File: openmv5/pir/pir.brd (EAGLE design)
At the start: 35.6 x 26.7 mm, 57 parts, among them IC1 AP3032KTR-G1, IC2 AP3032KTR-G1, J1 OPENMV5-TOP, Q1 2N7002KW_R1_00001, U1 EKMB1307113K, U2 MIC5365-3.3YMT-TZ

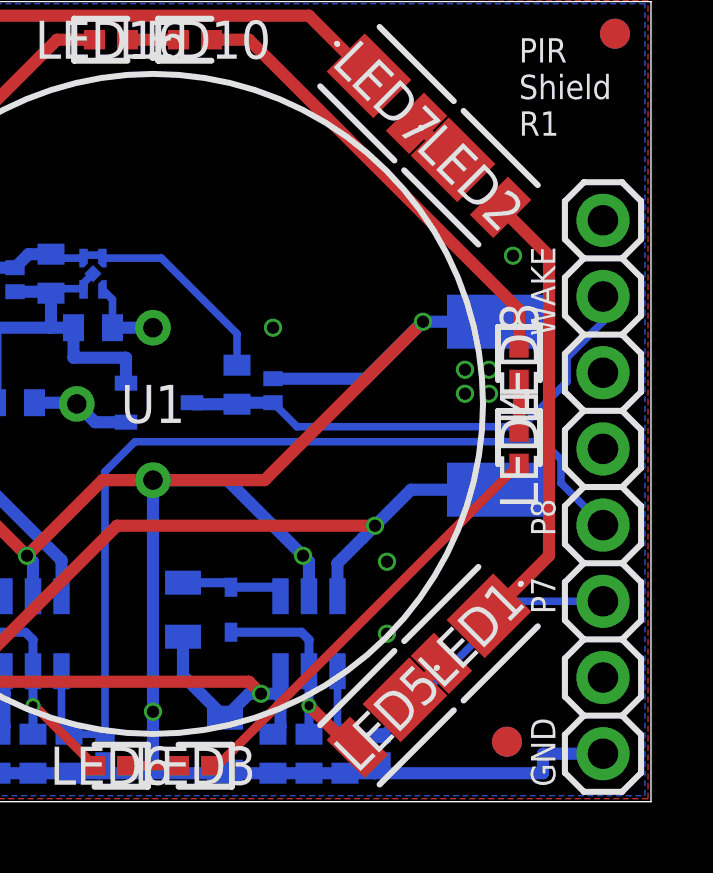
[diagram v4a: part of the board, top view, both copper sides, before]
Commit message: Add bypasses
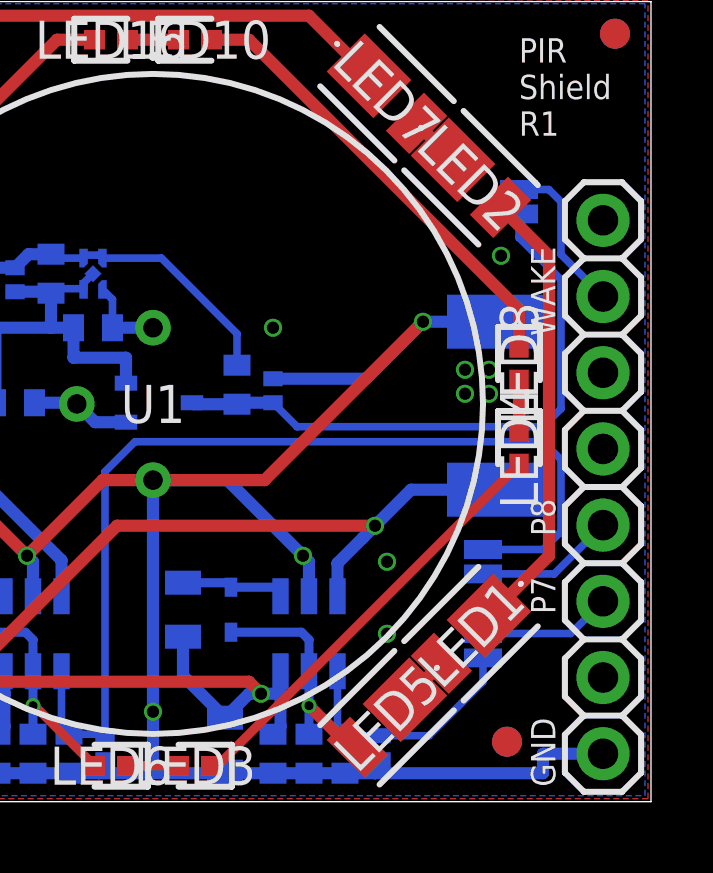
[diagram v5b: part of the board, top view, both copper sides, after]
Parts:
- added JP1, JP2, JP3: JUMPER-SMT_2_NC_PASTE_SILK, SparkFun-Jumpers:SMT-JUMPER_2_NC_PASTE_SILK
- moved U$1 18.1 mm to (16.4, 8.80)
- moved U$2 17.3 mm to (24.0, 8.00)
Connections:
- new net P11_WAKEUP_INT: J1.15, JP3.1
- new net P7_PWM_INT: J1.11, JP1.1
- new net P8_PWM_INT: J1.12, JP2.1
- net P11_WAKEUP: now also JP3.2; no longer J1.15
- net P7_PWM: now also JP1.2; no longer J1.11
- net P8_PWM: now also JP2.2; no longer J1.12
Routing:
- net P11_WAKEUP_INT: track 0.00 -> 5.31 mm
- net P8_PWM_INT: track 0.00 -> 4.67 mm
- net P7_PWM_INT: track 0.00 -> 4.44 mm
- net P7_PWM: track 12.7 -> 8.36 mm
- net P11_WAKEUP: track 16.8 -> 20.0 mm
- net P8_PWM: track 30.8 -> 33.3 mm
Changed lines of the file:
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@@
 <text x="10.8" y="14" size="0.8128" layer="22" font="vector" ratio="20" rot="MR270">Hot</text>
 <text x="27.2" y="12" size="0.8128" layer="22" font="vector" ratio="20" rot="MR90">Hot</text>
+<text x="28.6" y="6" size="0.8128" layer="22" font="vector" ratio="22" rot="MR270">P7</text>
+<text x="28.6" y="8.8" size="0.8128" layer="22" font="vector" ratio="22" rot="MR270">P8</text>
+<text x="29.9" y="21.5" size="0.8128" layer="22" font="vector" ratio="22" rot="MR270">WAKE</text>
 </plain>
 <attributes>
@@
 <element name="J1" library="openmv5" package="OPENMV5-TOP" value="OPENMV5-TOP" x="0" y="0" smashed="yes"/>
 <element name="U$9" library="openmv" package="OPENMV-LOGO" value="OPENMV-LOGO" x="1.4" y="22.6" smashed="yes"/>
-<element name="U$1" library="openmv" package="WEEE" value="" x="31.2" y="19.2" smashed="yes" rot="MR0"/>
-<element name="U$2" library="openmv" package="ROHS" value="" x="10.8" y="19.2" smashed="yes" rot="MR0"/>
+<element name="U$1" library="openmv" package="WEEE" value="" x="16.4" y="8.8" smashed="yes" rot="MR0"/>
+<element name="U$2" library="openmv" package="ROHS" value="" x="24" y="8" smashed="yes" rot="MR0"/>
 <element name="U$3" library="openmv" package="OMV-LOGO" value="" x="25.2" y="22" smashed="yes" rot="MR0"/>
 <element name="FD1" library="SparkFun-Aesthetics" library_urn="urn:adsk.eagle:library:507" package="FIDUCIAL-1X2" package3d_urn="urn:adsk.eagle:package:37108/1" value="FIDUCIAL1X2" x="7.4" y="2" smashed="yes"/>
@@
 <attribute name="NAME" x="6.8" y="11.8" size="1.27" layer="25" rot="R90" align="center"/>
 <attribute name="VALUE" x="6.8" y="11.8" size="1.27" layer="27" rot="R90" align="center"/>
+</element>
+<element name="JP1" library="SparkFun-Jumpers" library_urn="urn:adsk.eagle:library:528" package="SMT-JUMPER_2_NC_PASTE_SILK" package3d_urn="urn:adsk.eagle:package:39282/1" value="JUMPER-SMT_2_NC_PASTE_SILK" x="30" y="5.2" smashed="yes" rot="MR270">
+<attribute name="NAME" x="28.857" y="5.2" size="0.6096" layer="26" font="vector" ratio="20" rot="MR270" align="bottom-center"/>
+<attribute name="VALUE" x="31.143" y="5.2" size="0.6096" layer="28" font="vector" ratio="20" rot="MR270" align="top-center"/>
+</element>
+<element name="JP2" library="SparkFun-Jumpers" library_urn="urn:adsk.eagle:library:528" package="SMT-JUMPER_2_NC_PASTE_SILK" package3d_urn="urn:adsk.eagle:package:39282/1" value="JUMPER-SMT_2_NC_PASTE_SILK" x="30" y="8" smashed="yes" rot="MR90">
+<attribute name="NAME" x="31.143" y="8" size="0.6096" layer="26" font="vector" ratio="20" rot="MR90" align="bottom-center"/>
+<attribute name="VALUE" x="28.857" y="8" size="0.6096" layer="28" font="vector" ratio="20" rot="MR90" align="top-center"/>
+</element>
+<element name="JP3" library="SparkFun-Jumpers" library_urn="urn:adsk.eagle:library:528" package="SMT-JUMPER_2_NC_PASTE_SILK" package3d_urn="urn:adsk.eagle:package:39282/1" value="JUMPER-SMT_2_NC_PASTE_SILK" x="31.2" y="20" smashed="yes" rot="MR270">
+<attribute name="NAME" x="30.057" y="20" size="0.6096" layer="26" font="vector" ratio="20" rot="MR270" align="bottom-center"/>
+<attribute name="VALUE" x="32.343" y="20" size="0.6096" layer="28" font="vector" ratio="20" rot="MR270" align="top-center"/>
 </element>
 </elements>
@@
 <via x="19" y="3" extent="1-16" drill="0.4064"/>
 <via x="7" y="18.2" extent="1-16" drill="0.4064"/>
-<via x="31" y="18.2" extent="1-16" drill="0.4064"/>
+<via x="30.6" y="18.2" extent="1-16" drill="0.4064"/>
 <via x="7.8" y="14.4" extent="1-16" drill="0.4064"/>
 <via x="7.8" y="13.6" extent="1-16" drill="0.4064"/>
@@
 <contactref element="Q1" pad="3"/>
 <contactref element="D6" pad="1"/>
-<contactref element="J1" pad="15"/>
 <wire x1="21.8" y1="13.25" x2="20.35" y2="13.25" width="0.4064" layer="16"/>
 <wire x1="20.35" y1="13.25" x2="20.3" y2="13.3" width="0.4064" layer="16"/>
 <wire x1="23" y1="13.3" x2="21.85" y2="13.3" width="0.4064" layer="16"/>
 <wire x1="21.85" y1="13.3" x2="21.8" y2="13.25" width="0.4064" layer="16"/>
-<wire x1="31.3" y1="12.5" x2="23.8" y2="12.5" width="0.254" layer="16"/>
+<wire x1="32" y1="12.5" x2="23.8" y2="12.5" width="0.254" layer="16"/>
 <wire x1="23.8" y1="12.5" x2="23" y2="13.3" width="0.254" layer="16"/>
-<wire x1="31.3" y1="12.5" x2="32.8" y2="14" width="0.254" layer="16"/>
-<wire x1="32.8" y1="14" x2="32.8" y2="14.8" width="0.254" layer="16"/>
-<wire x1="34" y1="16.84" x2="34" y2="16" width="0.254" layer="16"/>
-<wire x1="34" y1="16" x2="32.8" y2="14.8" width="0.254" layer="16"/>
+<wire x1="32" y1="12.5" x2="32.6" y2="13.1" width="0.254" layer="16"/>
+<contactref element="JP3" pad="2"/>
+<wire x1="32.6" y1="13.1" x2="32.6" y2="17.4" width="0.254" layer="16"/>
+<wire x1="32.6" y1="17.4" x2="31.2" y2="18.8" width="0.254" layer="16"/>
+<wire x1="31.2" y1="19.5936" x2="31.2" y2="18.8" width="0.254" layer="16"/>
 </signal>
 <signal name="P7_PWM" class="4">
@@
 <contactref element="R1" pad="1"/>
 <contactref element="D3" pad="1"/>
-<contactref element="J1" pad="11"/>
 <wire x1="26.6" y1="2.2" x2="25.45" y2="2.2" width="0.254" layer="16"/>
 <wire x1="25.45" y1="2.2" x2="25.4" y2="2.25" width="0.254" layer="16"/>
 <wire x1="25.15" y1="4.35" x2="25.15" y2="2.5" width="0.254" layer="16"/>
 <wire x1="25.15" y1="2.5" x2="25.4" y2="2.25" width="0.254" layer="16"/>
-<wire x1="26.6" y1="2.2" x2="31.08" y2="6.68" width="0.254" layer="16"/>
-<wire x1="31.08" y1="6.68" x2="34" y2="6.68" width="0.254" layer="16"/>
+<contactref element="JP1" pad="2"/>
+<wire x1="26.6" y1="2.2" x2="28.2" y2="2.2" width="0.254" layer="16"/>
+<wire x1="28.2" y1="2.2" x2="30" y2="4" width="0.254" layer="16"/>
+<wire x1="30" y1="4" x2="30" y2="4.7936" width="0.254" layer="16"/>
 </signal>
 <signal name="VCC" class="3">
@@
 </signal>
 <signal name="P8_PWM" class="4">
-<contactref element="J1" pad="12"/>
 <contactref element="IC2" pad="4"/>
 <contactref element="R3" pad="1"/>
@@
 <wire x1="32.6" y1="11.4" x2="32" y2="12" width="0.254" layer="16"/>
 <wire x1="18.4" y1="12" x2="32" y2="12" width="0.254" layer="16"/>
-<wire x1="34" y1="9.22" x2="32.6" y2="10.62" width="0.254" layer="16"/>
-<wire x1="32.6" y1="10.62" x2="32.6" y2="11.4" width="0.254" layer="16"/>
+<contactref element="JP2" pad="2"/>
+<wire x1="30" y1="8.4064" x2="32.0064" y2="8.4064" width="0.254" layer="16"/>
+<wire x1="32.0064" y1="8.4064" x2="32.6" y2="9" width="0.254" layer="16"/>
+<wire x1="32.6" y1="9" x2="32.6" y2="11.4" width="0.254" layer="16"/>
 </signal>
 <signal name="WSW" class="3">
@@
 <wire x1="18.15" y1="1.2" x2="19.85" y2="1.2" width="0.3048" layer="1"/>
 </signal>
+<signal name="P7_PWM_INT" class="4">
+<contactref element="J1" pad="11"/>
+<contactref element="JP1" pad="1"/>
+<wire x1="30" y1="5.6064" x2="32.9264" y2="5.6064" width="0.254" layer="16"/>
+<wire x1="32.9264" y1="5.6064" x2="34" y2="6.68" width="0.254" layer="16"/>
+</signal>
+<signal name="P8_PWM_INT" class="4">
+<contactref element="J1" pad="12"/>
+<contactref element="JP2" pad="1"/>
+<wire x1="30" y1="7.5936" x2="32.3736" y2="7.5936" width="0.254" layer="16"/>
+<wire x1="32.3736" y1="7.5936" x2="34" y2="9.22" width="0.254" layer="16"/>
+</signal>
+<signal name="P11_WAKEUP_INT" class="4">
+<contactref element="J1" pad="15"/>
+<contactref element="JP3" pad="1"/>
+<wire x1="31.2" y1="20.4064" x2="32.1936" y2="20.4064" width="0.254" layer="16"/>
+<wire x1="32.6" y1="18.24" x2="34" y2="16.84" width="0.254" layer="16"/>
+<wire x1="32.1936" y1="20.4064" x2="32.6" y2="20" width="0.254" layer="16"/>
+<wire x1="32.6" y1="20" x2="32.6" y2="18.24" width="0.254" layer="16"/>
+</signal>
 </signals>
